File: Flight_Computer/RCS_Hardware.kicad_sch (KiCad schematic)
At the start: 54 parts, among them J1 SWD, J2 TYPE-C-31-M-12, J4 5V, J5 GND, J6 Solenoids, J7 Ext Sesnor, J8 Conn_01x05_Male, U1 STM32F401CCU6, U2 AMS1117-3.3, U3 BMP280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

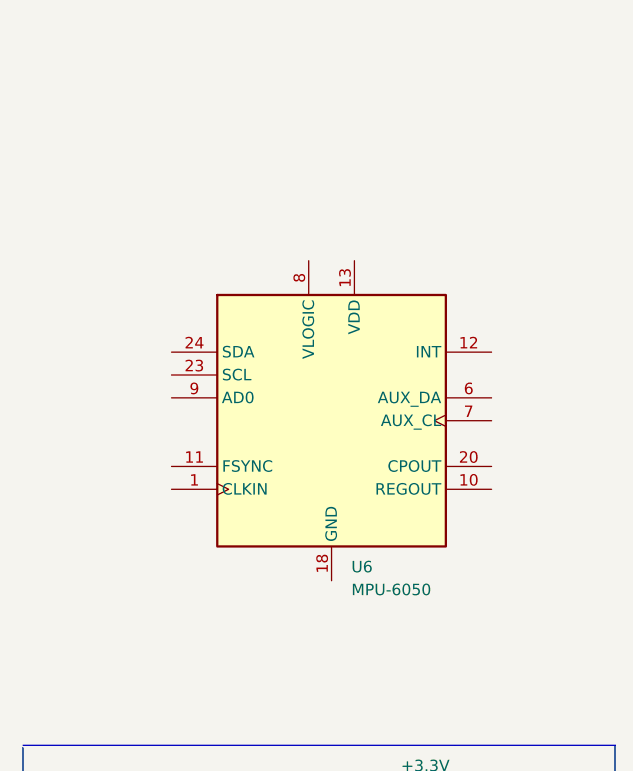
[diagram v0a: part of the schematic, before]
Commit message: Add Connections to MPU
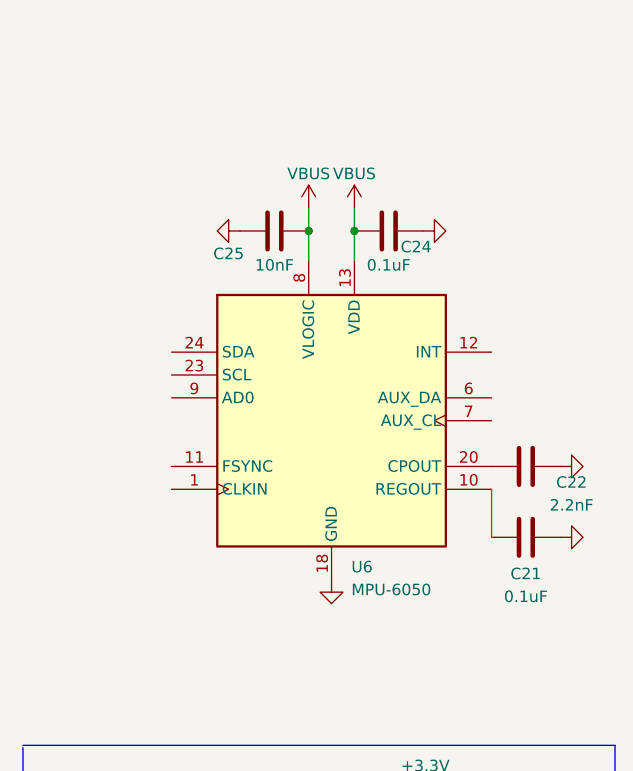
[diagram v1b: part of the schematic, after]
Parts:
- added C21, C24: 0.1uF, symbol Device:C
- added C22: 2.2nF, symbol Device:C
- added C25: 10nF, symbol Device:C
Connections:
- net GND: now also U6.18 (GND), C21.2, C22.2, C24.2, C25.1
- net VBUS: now also U6.13 (VDD), U6.8 (VLOGIC), C24.1, C25.2
- net at U6.10 (REGOUT): now also C21.1
- net at U6.20 (CPOUT): now also C22.1

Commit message: Added MPU Pin
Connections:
- net SCL: now also U6.23 (SCL)
- net SDA: now also U6.24 (SDA)
- net CLKIN: now reaches U6.1 (CLKIN)
- net FSYNC: now reaches U6.11 (FSYNC)
- net INT: now reaches U6.12 (INT)
- net AUX_DA: now reaches U6.6 (AUX_DA)
- net AUX_CL: now reaches U6.7 (AUX_CL)
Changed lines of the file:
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@@
   (junction (at 204.47 76.962) (diameter 0) (color 0 0 0 0)
   )
+  (junction (at 332.486 123.698) (diameter 0) (color 0 0 0 0)
+  )
   (junction (at 362.458 195.326) (diameter 0) (color 0 0 0 0)
   )
@@
     (stroke (width 0) (type default))
   )
+  (wire (pts (xy 327.152 123.698) (xy 332.486 123.698))
+    (stroke (width 0) (type default))
+  )
   (wire (pts (xy 119.888 35.814) (xy 119.888 47.244))
     (stroke (width 0) (type default))
@@
     (stroke (width 0) (type default))
   )
+  (wire (pts (xy 368.046 108.458) (xy 372.872 108.458))
+    (stroke (width 0) (type default))
+  )
   (wire (pts (xy 204.978 33.274) (xy 210.058 33.274))
     (stroke (width 0) (type default))
   )
+  (wire (pts (xy 326.898 108.458) (xy 332.486 108.458))
+    (stroke (width 0) (type default))
+  )
   (wire (pts (xy 360.172 220.726) (xy 362.204 220.726))
     (stroke (width 0) (type default))
@@
     (stroke (width 0) (type default))
   )
+  (wire (pts (xy 368.046 116.078) (xy 373.126 116.078))
+    (stroke (width 0) (type default))
+  )
   (wire (pts (xy 378.46 195.326) (xy 378.46 208.026))
     (stroke (width 0) (type default))
@@
     (stroke (width 0) (type default))
   )
+  (wire (pts (xy 332.486 121.158) (xy 327.152 121.158))
+    (stroke (width 0) (type default))
+  )
   (wire (pts (xy 319.786 167.132) (xy 332.232 167.132))
     (stroke (width 0) (type default))
@@
     (stroke (width 0) (type default))
   )
+  (wire (pts (xy 326.898 110.998) (xy 332.486 110.998))
+    (stroke (width 0) (type default))
+  )
   (wire (pts (xy 109.728 30.734) (xy 109.728 43.434))
     (stroke (width 0) (type default))
@@
     (stroke (width 0) (type default))
   )
+  (wire (pts (xy 368.046 113.538) (xy 373.126 113.538))
+    (stroke (width 0) (type default))
+  )
   (wire (pts (xy 136.906 29.464) (xy 143.256 29.464))
     (stroke (width 0) (type default))
@@
     (stroke (width 0) (type default))
   )
+  (wire (pts (xy 327.152 121.158) (xy 327.152 121.412))
+    (stroke (width 0) (type default))
+  )
   (wire (pts (xy 93.726 108.204) (xy 98.298 108.204))
     (stroke (width 0) (type default))
@@
     (stroke (width 0) (type default))
   )
+  (wire (pts (xy 326.898 113.284) (xy 332.74 113.284))
+    (stroke (width 0) (type default))
+  )
   (wire (pts (xy 87.63 100.584) (xy 98.298 100.584))
     (stroke (width 0) (type default))
@@
     (stroke (width 0) (type default))
   )
+  (wire (pts (xy 332.486 123.698) (xy 332.74 123.698))
+    (stroke (width 0) (type default))
+  )
   (wire (pts (xy 161.29 254) (xy 161.29 256.032))
     (stroke (width 0) (type default))
@@
     (effects (font (size 1.27 1.27)) (justify right bottom))
   )
+  (label "FSYNC" (at 327.152 121.412 0) (fields_autoplaced)
+    (effects (font (size 1.27 1.27)) (justify left bottom))
+  )
   (label "USB_D-" (at 140.716 113.284 180) (fields_autoplaced)
     (effects (font (size 1.27 1.27)) (justify right bottom))
@@
     (effects (font (size 1.27 1.27)) (justify left bottom))
   )
+  (label "INT" (at 372.872 108.458 0) (fields_autoplaced)
+    (effects (font (size 1.27 1.27)) (justify left bottom))
+  )
   (label "BNO_NRST" (at 87.63 100.584 0) (fields_autoplaced)
     (effects (font (size 1.27 1.27)) (justify left bottom))
@@
     (effects (font (size 1.27 1.27)) (justify left bottom))
   )
+  (label "CLKIN" (at 327.152 123.698 0) (fields_autoplaced)
+    (effects (font (size 1.27 1.27)) (justify left bottom))
+  )
   (label "OSC_OUT" (at 89.662 72.644 0) (fields_autoplaced)
     (effects (font (size 1.27 1.27)) (justify left bottom))
@@
     (effects (font (size 1.27 1.27)) (justify right bottom))
   )
+  (label "AD0" (at 326.898 113.284 0) (fields_autoplaced)
+    (effects (font (size 1.27 1.27)) (justify left bottom))
+  )
   (label "USB_D-" (at 250.952 70.612 0) (fields_autoplaced)
     (effects (font (size 1.27 1.27)) (justify left bottom))
@@
     (effects (font (size 1.27 1.27)) (justify left bottom))
   )
+  (label "AUX_CL" (at 373.126 116.078 0) (fields_autoplaced)
+    (effects (font (size 1.27 1.27)) (justify left bottom))
+  )
   (label "SDA" (at 93.726 105.664 0) (fields_autoplaced)
     (effects (font (size 1.27 1.27)) (justify left bottom))
@@
     (effects (font (size 1.27 1.27)) (justify right bottom))
   )
+  (label "AUX_DA" (at 373.126 113.538 0) (fields_autoplaced)
+    (effects (font (size 1.27 1.27)) (justify left bottom))
+  )
   (label "S1" (at 134.112 87.884 180) (fields_autoplaced)
     (effects (font (size 1.27 1.27)) (justify right bottom))
@@
     (effects (font (size 1 1)) (justify left bottom))
   )
+  (label "SDA" (at 326.898 108.458 0) (fields_autoplaced)
+    (effects (font (size 1.27 1.27)) (justify left bottom))
+  )
   (label "BNO_NRST" (at 319.532 195.326 0) (fields_autoplaced)
     (effects (font (size 1.27 1.27)) (justify left bottom))
@@
     (effects (font (size 1.27 1.27)) (justify right bottom))
   )
+  (label "SCL" (at 326.898 110.998 0) (fields_autoplaced)
+    (effects (font (size 1.27 1.27)) (justify left bottom))
+  )
   (label "RX" (at 135.8772 90.424 180) (fields_autoplaced)
     (effects (font (size 1.27 1.27)) (justify right bottom))
@@
     (pin "3")
     (pin "4")
-    (pin "8")
-    (pin "7")
-    (pin "6")
     (pin "5")
+    (pin "6")
+    (pin "7")
+    (pin "8")
     (instances
       (project "RCS_Hardware"
@@
       (effects (font (size 1.27 1.27)) hide)
     )
-    (pin "14")
-    (pin "13")
-    (pin "12")
-    (pin "11")
+    (pin "1")
     (pin "10")
+    (pin "11")
+    (pin "12")
+    (pin "13")
+    (pin "14")
     (pin "15")
-    (pin "1")
     (pin "16")
     (pin "17")

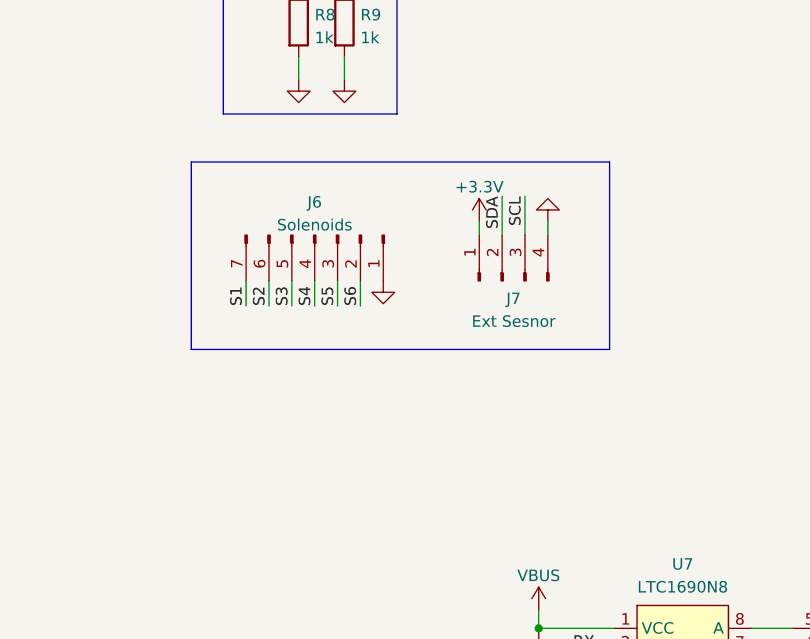
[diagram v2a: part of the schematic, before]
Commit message: Added SPI/CS pins
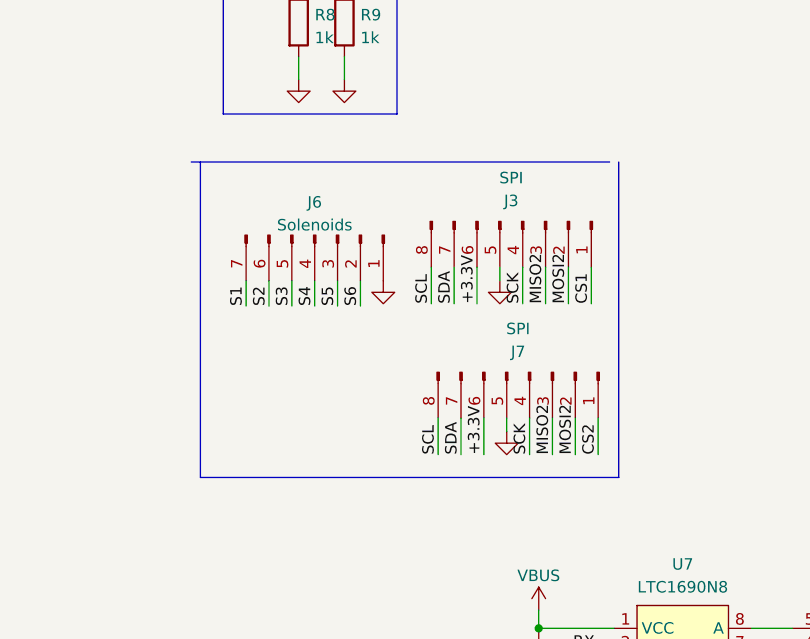
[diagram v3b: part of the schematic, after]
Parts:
- removed J7: Ext Sesnor, Connector_PinHeader_2.54mm:PinHeader_1x04_P2.54mm_Vertical, symbol Connector:Conn_01x04_Male
- added J3, J7: SPI, symbol Connector:Conn_01x08_Pin
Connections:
- net +3.3V: now also J3.6 (Pin_6), J7.6 (Pin_6)
- net GND: now also J3.5 (Pin_5), J7.5 (Pin_5)
- net SCL: now also J3.8 (Pin_8), J7.8 (Pin_8)
- net SDA: now also J3.7 (Pin_7), J7.7 (Pin_7)
- new net CS1: J3.1 (Pin_1)
- new net CS2: J7.1 (Pin_1)
- new net MISO2: J3.3 (Pin_3), J7.3 (Pin_3)
- new net MOSI2: J3.2 (Pin_2), J7.2 (Pin_2)
- new net SCK: J3.4 (Pin_4), J7.4 (Pin_4)

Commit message: started new routing
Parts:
- removed C19: 100nF, Capacitor_SMD:C_0402_1005Metric, symbol Device:C
- removed R5, R6: 10k, Resistor_SMD:R_0402_1005Metric, symbol Device:R
- removed U3: BMP280, XDCR_BMP280, symbol BMP280:BMP280
- C21, C22, C24, C25: footprint (none) -> Capacitor_SMD:C_0402_1005Metric
- C4: footprint Capacitor_SMD:C_0603_1608Metric -> Capacitor_SMD:C_0402_1005Metric
- J3, J7: footprint (none) -> Connector_PinHeader_2.54mm:PinHeader_1x08_P2.54mm_Vertical
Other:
- note removed: "BMP280"

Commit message: more routing!
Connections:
- net AD0: now also U6.9 (AD0)
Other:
- moved on the sheet: C1, C10, C11, C12, C2, C3, C4, C5, C6, C7, C8, C9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
